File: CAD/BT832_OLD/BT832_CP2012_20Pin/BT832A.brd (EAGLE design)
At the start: 24.9 x 49.9 mm, 44 parts, among them U1 MCP73831T-3ACI/OT, U2 BT832, U3 LP5907MFX-3.3/NOPB, U4 LP5907MFX-3.3/NOPB, U5 ADS131M08IPBS, U6 BCM857BS, U7 CP2102N-A02-GQFN20R, X1 ABM3B-8.000MHZ-B2-T, X2 FC-12M

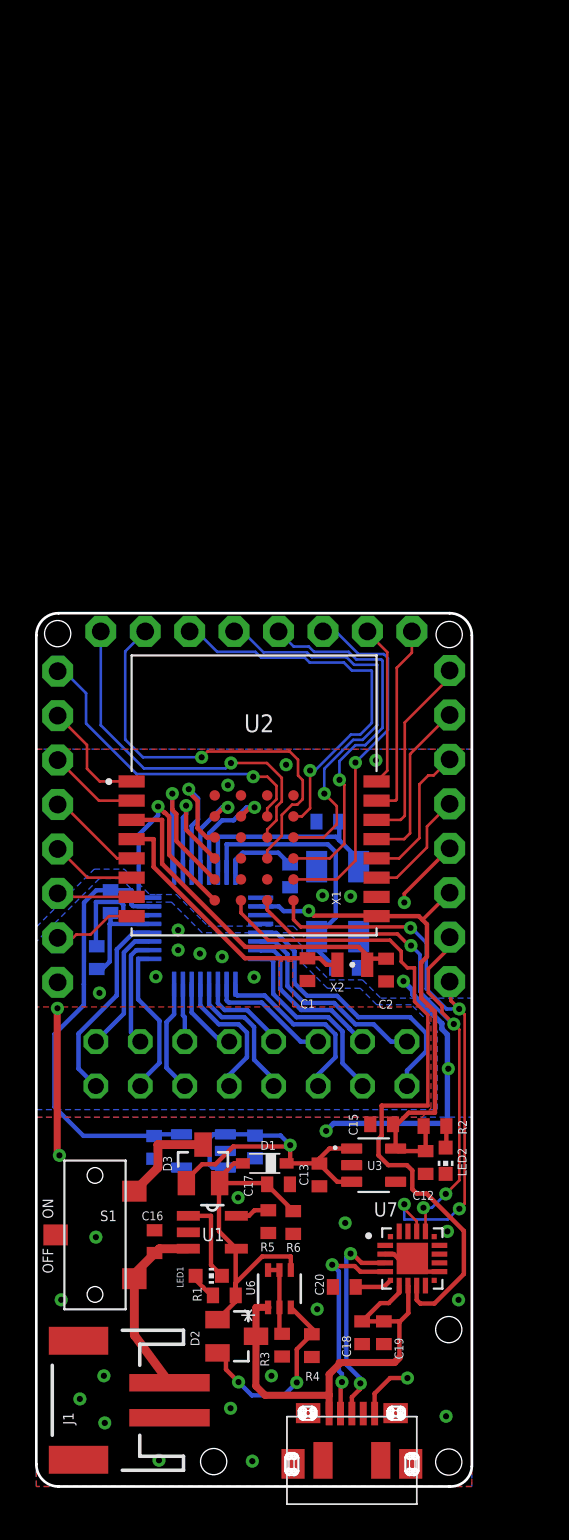
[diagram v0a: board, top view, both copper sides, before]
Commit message: added missing voltage divider (doesn't fix the battery charger circuit)
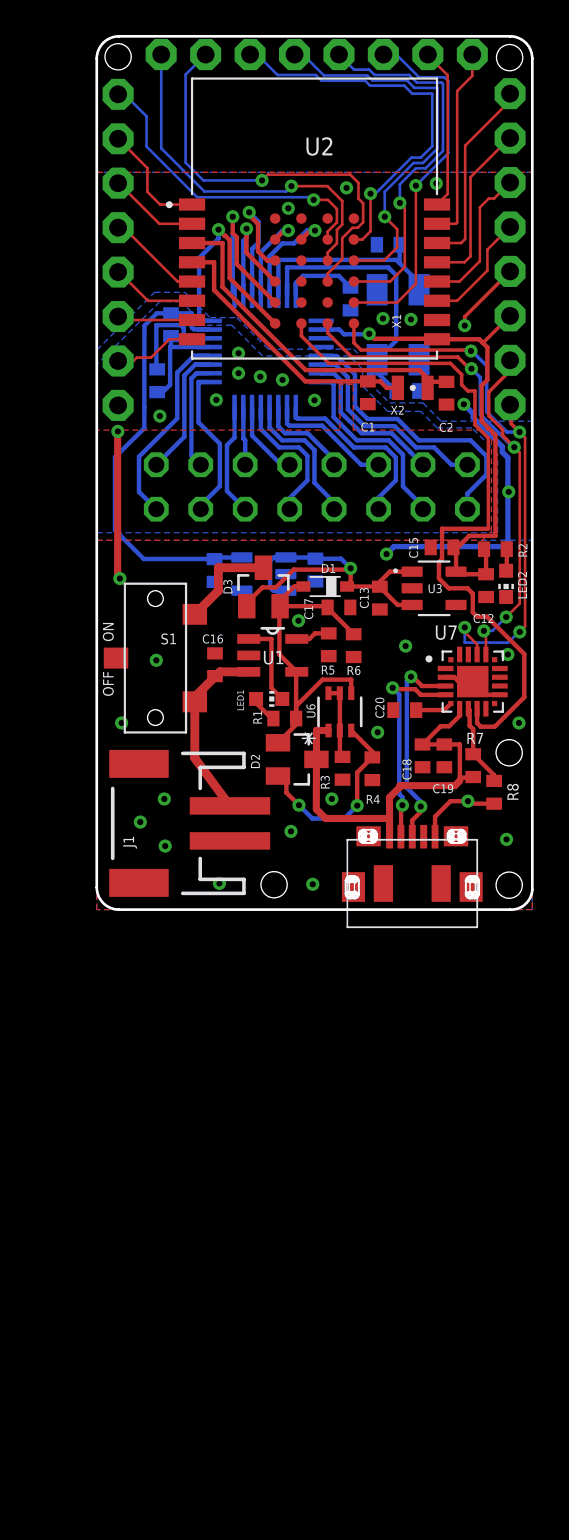
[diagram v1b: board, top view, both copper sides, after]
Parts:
- added R7: 24kΩ, adafruit:R0402
- added R8: 47kΩ, adafruit:R0402
- moved C1 33.1 mm to (25.6, 33.4)
- moved C12 33.1 mm to (32.3, 22.4)
- moved C13 33.1 mm to (26.2, 21.7)
- moved C15 33.1 mm to (29.8, 24.6)
- moved C16 33.1 mm to (16.8, 17.9)
- moved C17 33.1 mm to (23.9, 21.2)
- moved C18 33.1 mm to (28.7, 12.7)
- moved C19 33.1 mm to (29.9, 12.7)
- moved C2 33.1 mm to (30.0, 33.4)
- moved C20 33.1 mm to (27.7, 15.3)
- moved C3 33.1 mm to (27.8, 33.5)
- moved C4 33.1 mm to (26.7, 41.9)
- moved C5 33.1 mm to (14.3, 37.3)
- moved C6 33.1 mm to (24.6, 38.8)
- moved C7 33.1 mm to (22.6, 23.3)
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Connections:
- new net VBUS: R7.2, R8.2, U7.8
- net +5V: now also R7.1; no longer U7.8
- net GND: now also R8.1
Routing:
- net VBUS: track 0.00 -> 4.73 mm
- net GND: track 41.8 -> 43.4 mm
- net +5V: track 26.1 -> 24.5 mm
